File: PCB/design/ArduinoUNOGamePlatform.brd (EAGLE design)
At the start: 68.6 x 53.3 mm, 23 parts, among them J3 PJ-320D-A, Q1 ON_SEMICONDUCTOR_BC849BLT1GON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, Q2 ON_SEMICONDUCTOR_BC849BLT1GON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

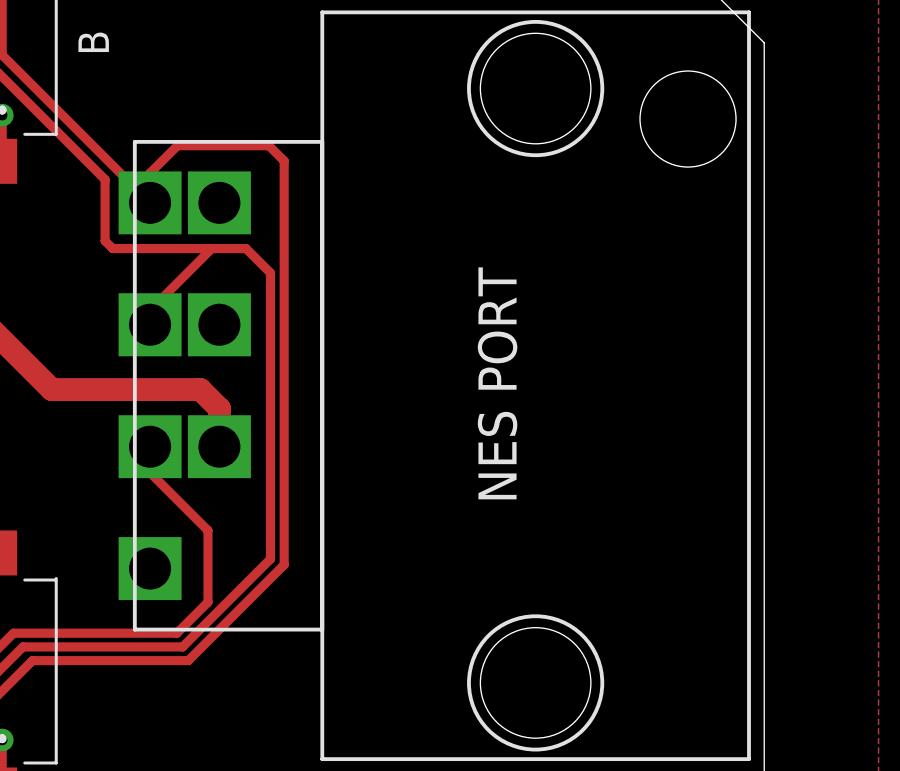
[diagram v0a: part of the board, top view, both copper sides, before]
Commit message: Fixed some stale comments and removed commented out old code. Changed some resistor values on PCB following testing. Added designation to move order number under the NES port if using JLC to produce board. Also changed pinouts for buttons to match buttons on shield (I had reversed the positions on PORTC!
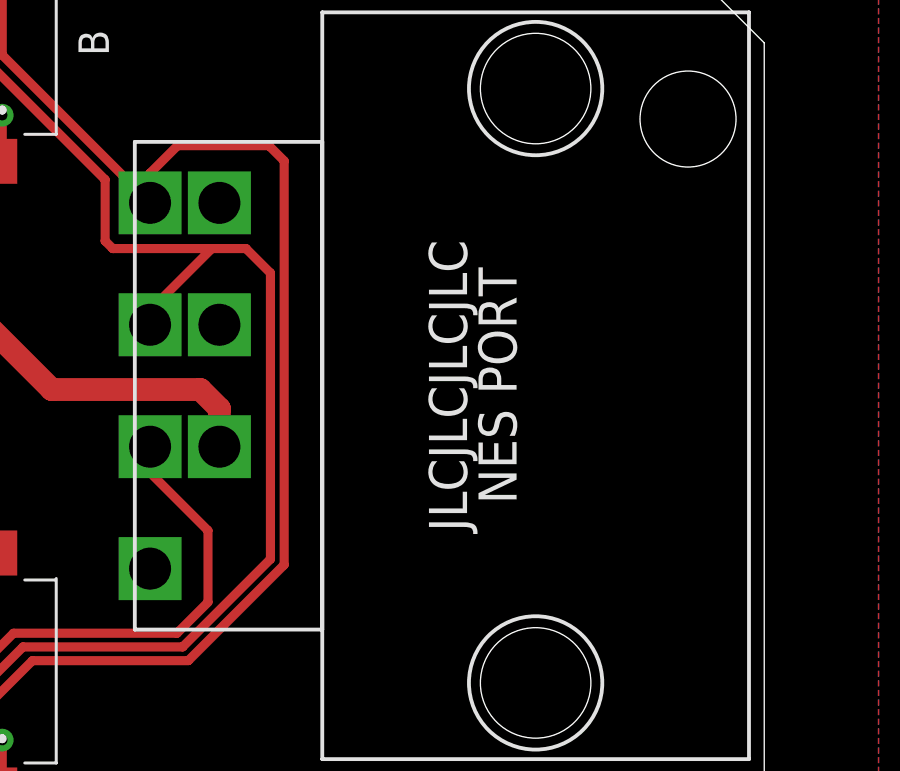
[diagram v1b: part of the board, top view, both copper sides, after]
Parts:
- R1: value DNP -> 75R
- R2: value 180R -> 220R
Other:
- board text added: "JLCJLCJLCJLC"
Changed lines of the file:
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@@
 <wire x1="7.62" y1="44.45" x2="6.985" y2="45.085" width="0.3048" layer="21"/>
 <wire x1="6.985" y1="45.085" x2="1.905" y2="45.085" width="0.3048" layer="21"/>
+<text x="58.674" y="26.67" size="1.27" layer="21" rot="R90" align="bottom-center">JLCJLCJLCJLC</text>
 </plain>
 <attributes>
@@
 <attribute name="VAULT_REVISION" value="B4675A61-FAF7-4072-9C56-0A9635A35669" x="16.129" y="15.748" size="1.778" layer="27" rot="R180" display="off"/>
 </element>
-<element name="R2" library="ESP32_DMX_Audio" library_urn="urn:adsk.eagle:library:21091620" package="52101-101-REV-A_RC-MASTER-SMD_R0603MP" package3d_urn="urn:adsk.eagle:package:21091780/2" value="180R" x="15.24" y="33.02" smashed="yes" rot="R270"/>
+<element name="R2" library="ESP32_DMX_Audio" library_urn="urn:adsk.eagle:library:21091620" package="52101-101-REV-A_RC-MASTER-SMD_R0603MP" package3d_urn="urn:adsk.eagle:package:21091780/2" value="220R" x="15.24" y="33.02" smashed="yes" rot="R270"/>
 <element name="R3" library="ESP32_DMX_Audio" library_urn="urn:adsk.eagle:library:21091620" package="52101-101-REV-A_RC-MASTER-SMD_R0603MP" package3d_urn="urn:adsk.eagle:package:21091780/2" value="1K2" x="12.954" y="33.02" smashed="yes" rot="R270"/>
 <element name="R8" library="ESP32_DMX_Audio" library_urn="urn:adsk.eagle:library:21091620" package="52101-101-REV-A_RC-MASTER-SMD_R0603MP" package3d_urn="urn:adsk.eagle:package:21091780/2" value="470R" x="18.669" y="15.748" smashed="yes" rot="R90"/>
@@
 <attribute name="MOUSER_PRICE-STOCK" value="" x="39.37" y="24.13" size="1.778" layer="27" rot="R90" display="off"/>
 </element>
-<element name="R1" library="ESP32_DMX_Audio" library_urn="urn:adsk.eagle:library:21091620" package="52101-101-REV-A_RC-MASTER-SMD_R0603MP" package3d_urn="urn:adsk.eagle:package:21091780/2" value="DNP" x="10.795" y="33.02" smashed="yes" rot="R90"/>
+<element name="R1" library="ESP32_DMX_Audio" library_urn="urn:adsk.eagle:library:21091620" package="52101-101-REV-A_RC-MASTER-SMD_R0603MP" package3d_urn="urn:adsk.eagle:package:21091780/2" value="75R" x="10.795" y="33.02" smashed="yes" rot="R90"/>
 <element name="U$3" library="PJ-320D-A" library_urn="urn:adsk.eagle:library:43570733" package="NES-CONTROLLER-SOCKET" package3d_urn="urn:adsk.eagle:package:43570976/2" value="NES-CONTROLLER-PORT" x="60.96" y="26.67" smashed="yes" rot="R270"/>
 </elements>

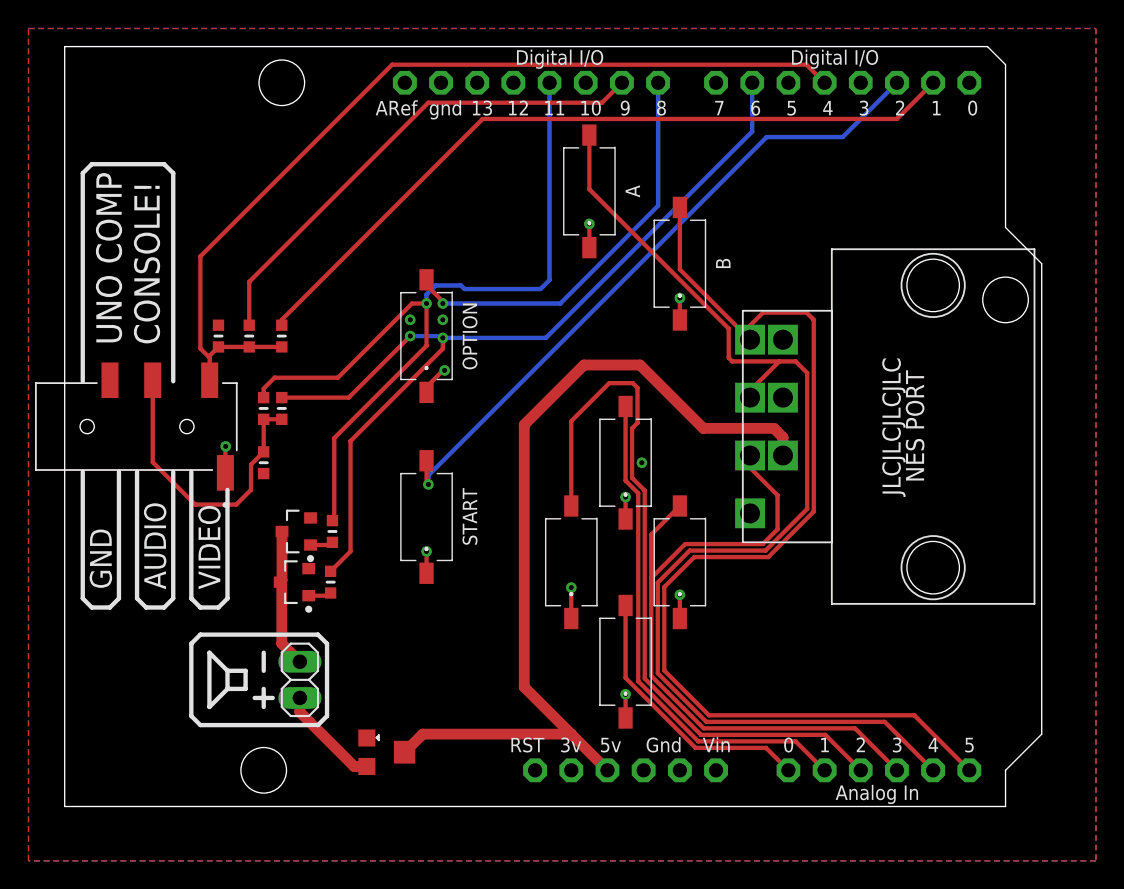
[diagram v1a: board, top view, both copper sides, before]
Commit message: Modified PCB design to make it easier for hand-soldering, and also changed to better buttons
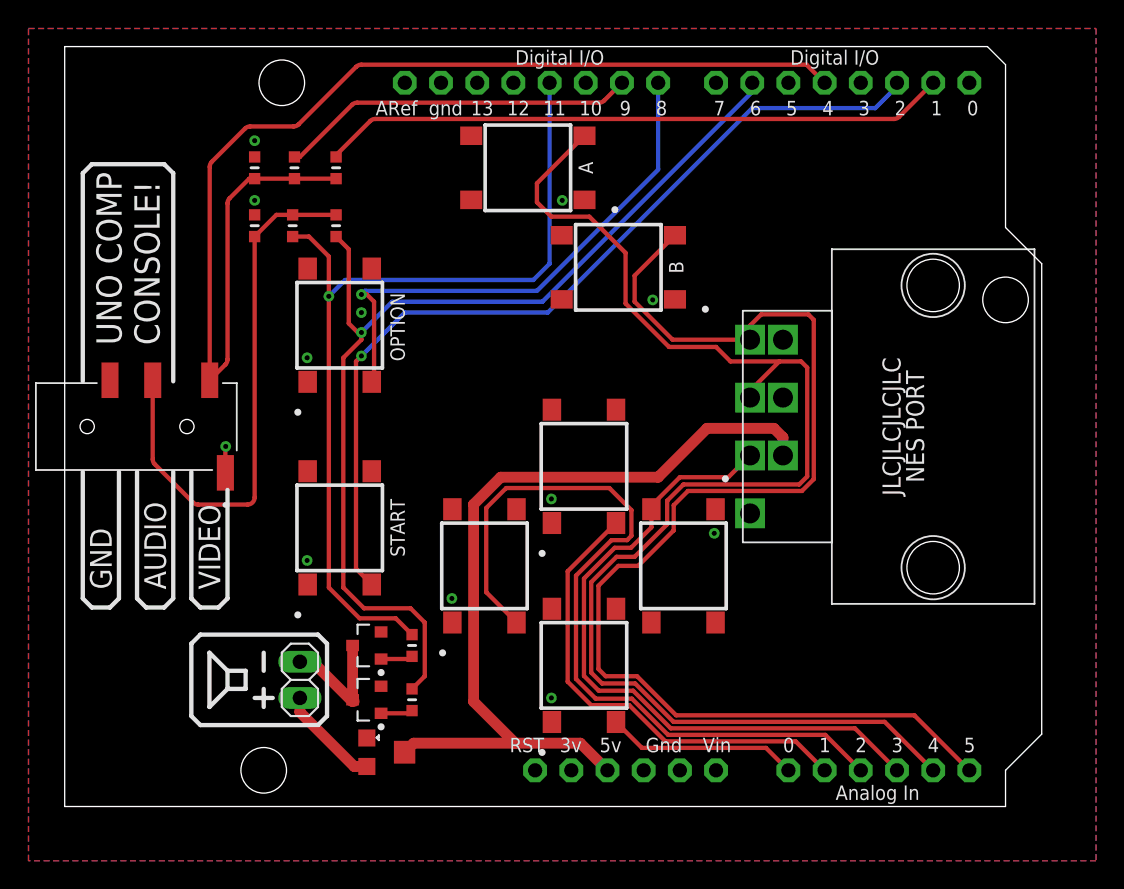
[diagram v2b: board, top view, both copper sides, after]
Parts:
- B1, B2, B3, B4, B5, B6, B7, B8: value K2-1107ST-A4SW-06 -> PTS645SM43SMTR92LFS; device K2-1107ST-A4SW-06:K21107STA4SW06 -> PTS645SM43SMTR92LFS:PTS645(SMT)
- moved B2 29.4 mm to (19.3, 19.6)
- moved B1 24.3 mm to (19.3, 33.8)
- moved B4 22.1 mm to (38.9, 37.8), turned to 180 degrees
- moved R6 16.6 mm to (13.3, 40.8), turned to 90 degrees
- moved B3 13.8 mm to (32.5, 44.8), turned to 180 degrees
- moved R5 13.4 mm to (19.1, 40.8), turned to 90 degrees
- moved R4 13.0 mm to (16.0, 40.8), turned to 90 degrees
- moved R2 12.4 mm to (19.1, 44.8)
- moved R3 12.2 mm to (16.1, 44.8)
- moved R1 12.1 mm to (13.3, 44.8)
- moved R8 10.0 mm to (24.4, 7.49)
- moved R7 9.76 mm to (24.4, 11.3)
- moved Q2 9.69 mm to (21.2, 7.49)
- moved B6 9.52 mm to (36.4, 23.9)
- moved Q1 9.41 mm to (21.2, 11.3)
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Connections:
- net BUT_A: now also B3.3; no longer B2.2
- net BUT_B: now also B4.3; no longer B1.2
- net BUT_DOWN: now also B8.3; no longer B6.2
- net BUT_LEFT: now also B7.3; no longer B7.2
- net BUT_OPTION: now also B1.3; no longer B3.2
- net BUT_RIGHT: now also B6.3; no longer B8.2
- net BUT_START: now also B2.3; no longer B4.2
- net BUT_UP: now also B5.3; no longer B5.2
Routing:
- net COMP_OUT: track 64.3 -> 83.0 mm
- net AUDIO_OUT: track 21.0 -> 38.9 mm
- net BUT_START: track 46.7 -> 62.3 mm
- net BUT_A: track 79.7 -> 95.3 mm
- net GND: track 15.8 -> 1.86 mm
- net BUT_B: track 73.7 -> 86.2 mm
- net SYNC_OUT: track 35.0 -> 25.1 mm
- net AUDB: track 63.9 -> 72.9 mm, vias 2 -> 1
- net VIDEO_OUT: track 53.0 -> 44.1 mm
- net BUT_OPTION: track 28.7 -> 37.3 mm
- net BUT_UP: track 50.6 -> 57.1 mm
- net AUDA: track 56.3 -> 62.7 mm
- net BUT_LEFT: track 19.2 -> 13.5 mm
- net VCC: track 62.2 -> 58.7 mm
- net BUT_RIGHT: track 35.3 -> 33.2 mm
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
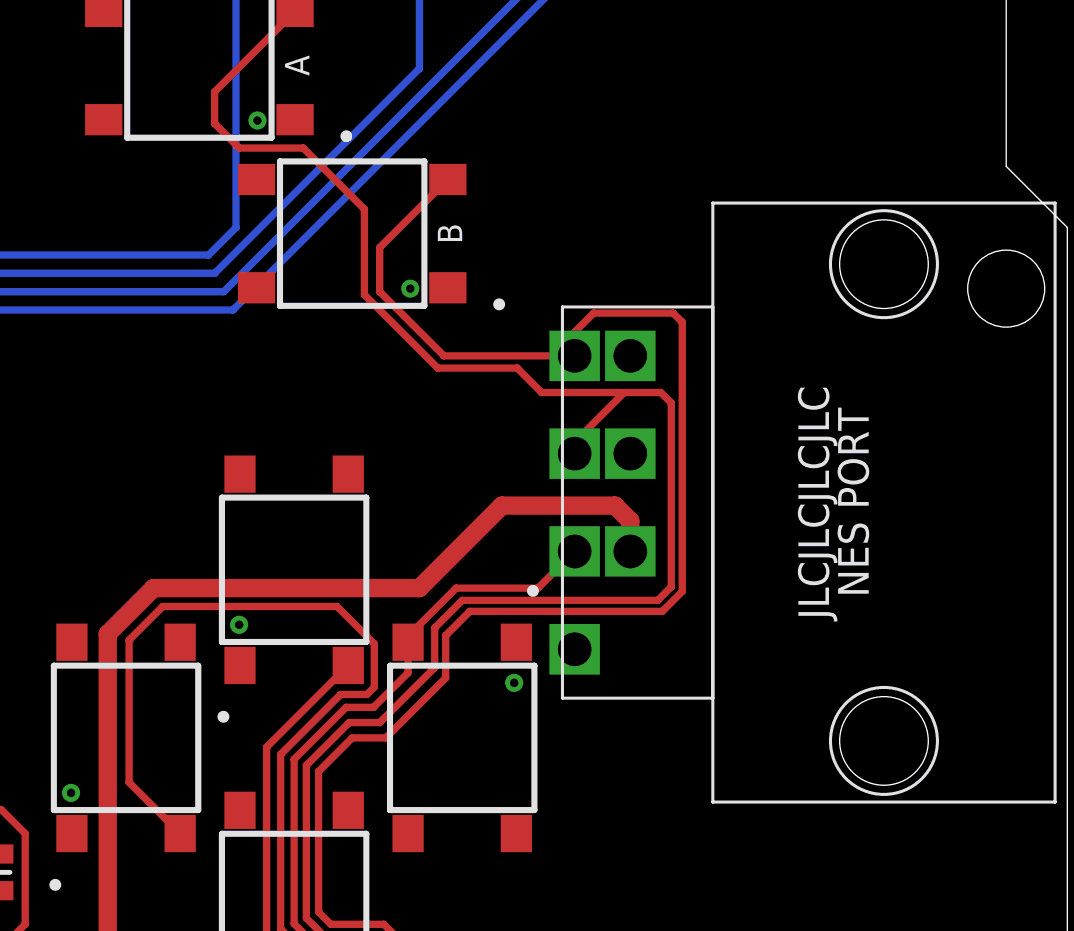
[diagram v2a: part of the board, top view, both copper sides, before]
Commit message: Updated PCB design to modify NES port part. Holes were too tight and not enough clearance for it under board, so now on top. Also pins moved slightly further apart to make soldering a little easier
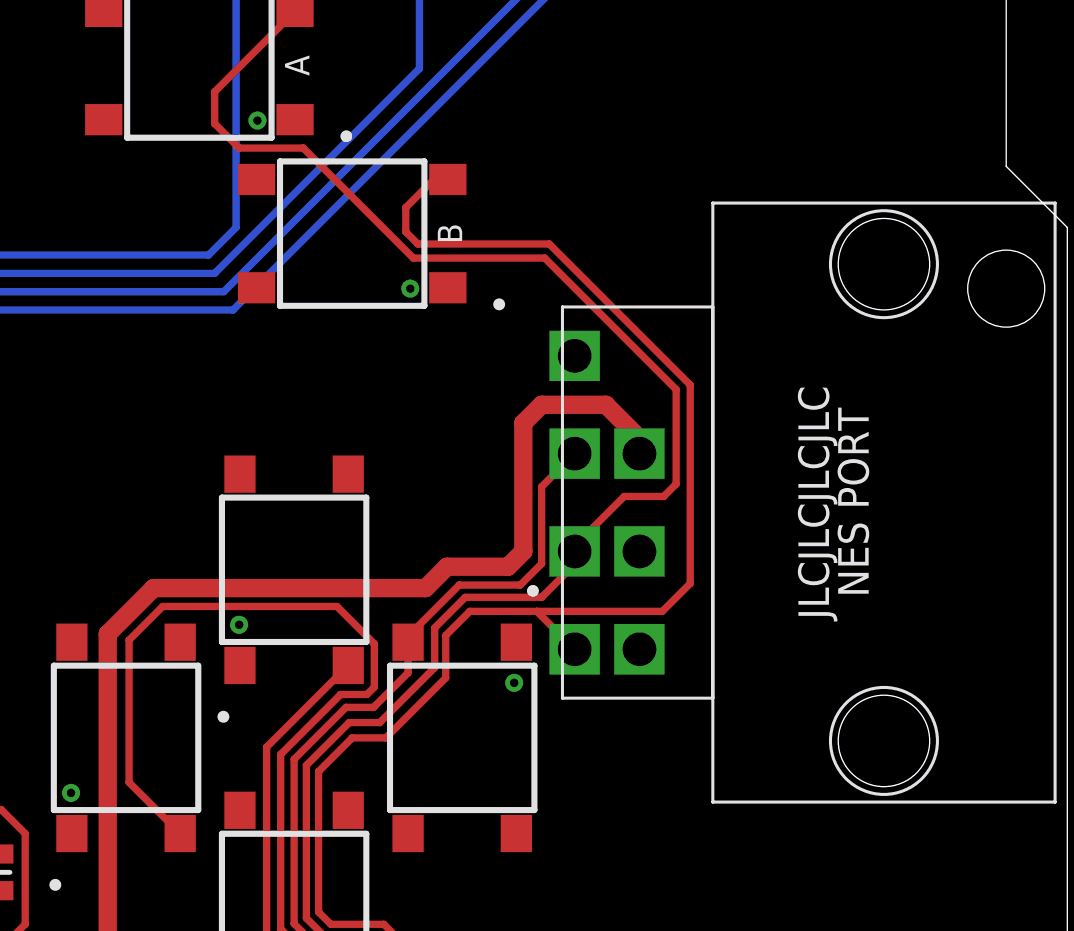
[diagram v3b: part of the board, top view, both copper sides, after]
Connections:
- net BUT_A: now also U$3.7; no longer U$3.2
- net BUT_B: now also U$3.8; no longer U$3.1
- net BUT_DOWN: now also U$3.6; no longer U$3.3
- net GND: now also U$3.5; no longer U$3.4
- net VCC: now also U$3.3; no longer U$3.6
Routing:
- net BUT_A: track 95.3 -> 88.5 mm
- net VCC: track 58.7 -> 63.6 mm
- net BUT_DOWN: track 47.7 -> 51.2 mm
- net BUT_B: track 86.2 -> 82.7 mm

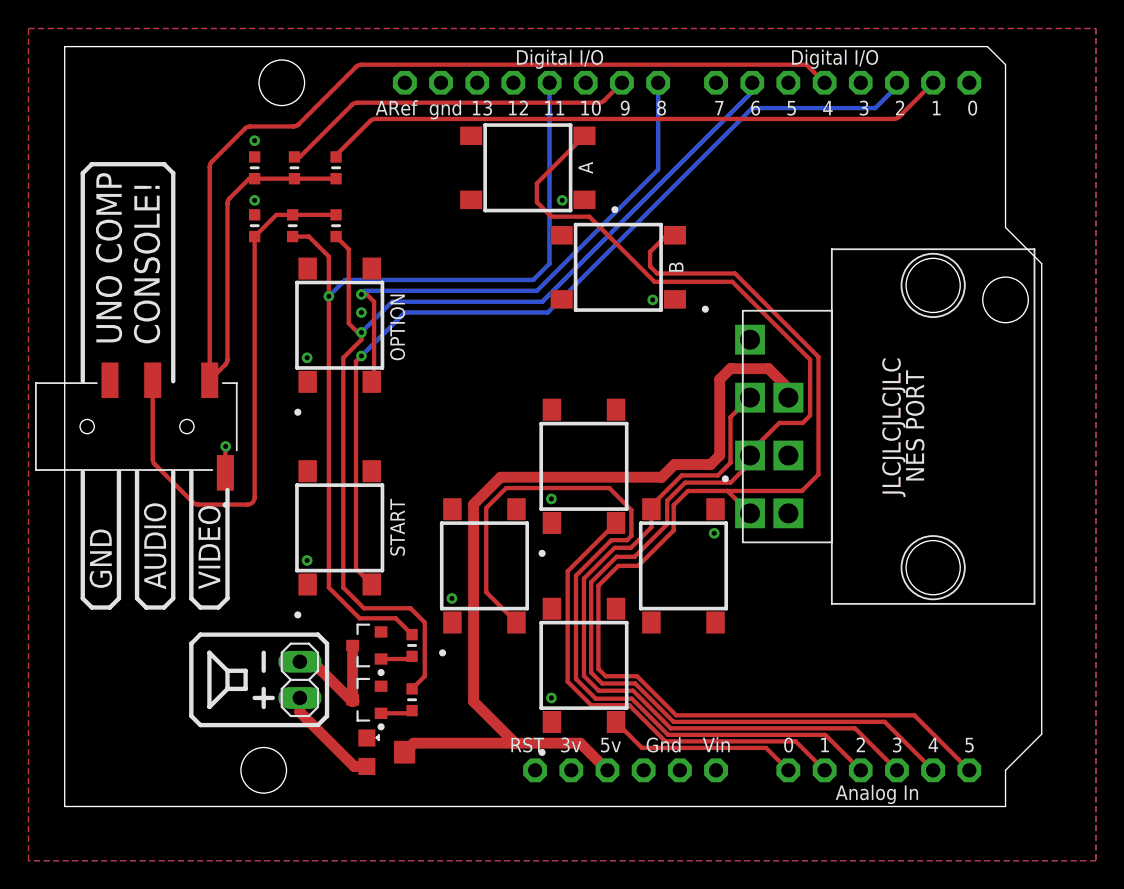
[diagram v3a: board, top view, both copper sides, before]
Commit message: Decided to move the pins used for the controller to unused pins on PORTB so that buttons could be used in addition, in future games. Also modified input a little to controller reading. New PCB images and schematic
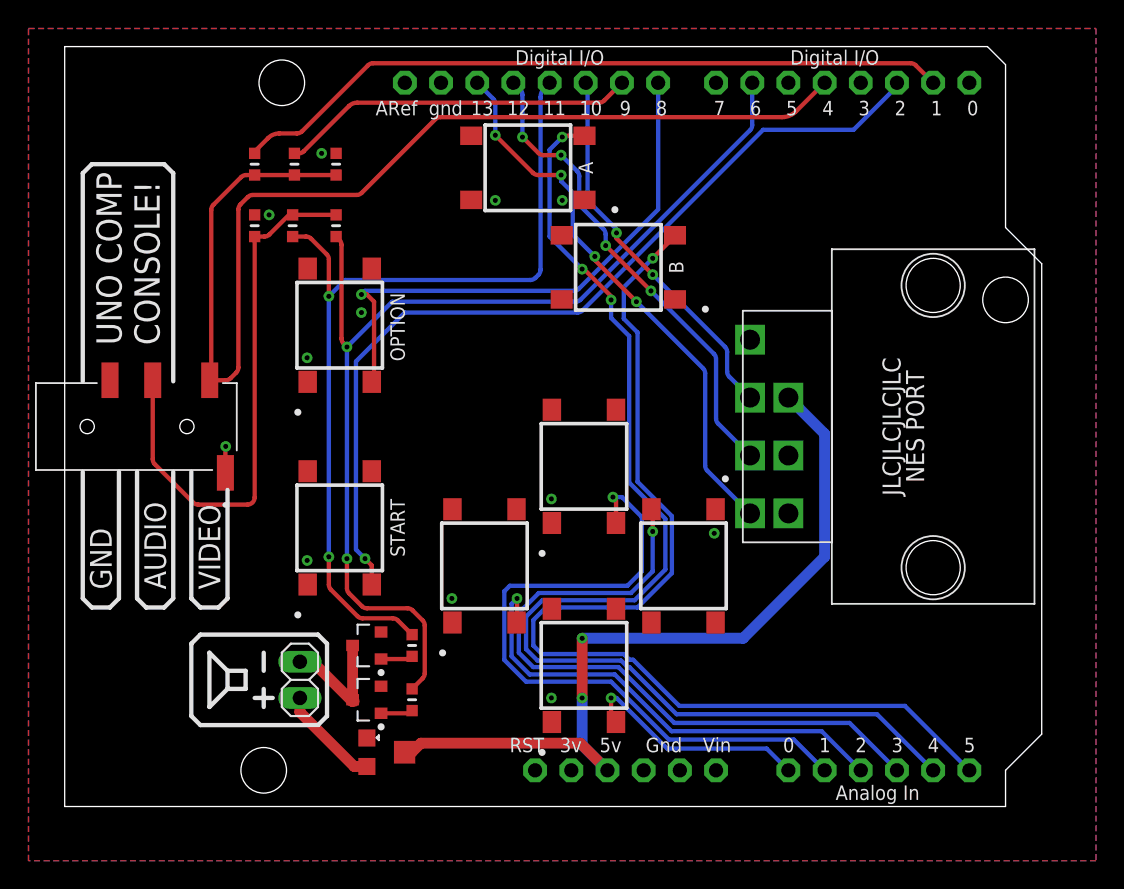
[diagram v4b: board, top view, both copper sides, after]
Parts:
- moved R1 5.72 mm to (19.1, 45.1)
- moved R2 5.72 mm to (13.3, 45.1)
- moved R3 0.25 mm to (16.1, 45.1)
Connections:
- new net NES_CLOCK: U$2.D10, U$3.6
- new net NES_DATA: U$2.D13, U$3.8
- new net NES_LATCH: U$2.D12, U$3.7
- net BUT_A: no longer U$3.7
- net BUT_B: no longer U$3.8
- net BUT_DOWN: no longer U$3.6
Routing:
- net NES_DATA: track 0.00 -> 39.0 mm, vias 0 -> 4
- net NES_LATCH: track 0.00 -> 33.7 mm, vias 0 -> 4
- net NES_CLOCK: track 0.00 -> 26.8 mm, vias 0 -> 2
- net BUT_UP: track 57.1 -> 33.8 mm, vias 0 -> 1
- net BUT_RIGHT: track 33.2 -> 49.1 mm, vias 0 -> 1
- net BUT_B: track 82.7 -> 73.7 mm, vias 0 -> 1
- net BUT_A: track 88.5 -> 81.3 mm, vias 0 -> 3
- net VCC: track 63.6 -> 56.9 mm, vias 0 -> 2
- net VIDEO_OUT: track 44.1 -> 50.7 mm
- net BUT_DOWN: track 51.2 -> 47.8 mm, vias 0 -> 1
- net BUT_LEFT: track 13.5 -> 16.4 mm, vias 0 -> 1
- net COMP_OUT: track 83.0 -> 80.1 mm
- net BUT_OPTION: track 37.3 -> 39.0 mm
- net AUDB: track 72.9 -> 74.3 mm, vias 1 -> 2
- net AUDA: track 62.7 -> 62.4 mm, vias 1 -> 2
